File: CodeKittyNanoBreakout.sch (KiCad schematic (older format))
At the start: 13 parts, among them P1 CONN_01X02, P2 CONN_01X02, P3 CONN_01X03, P4 CONN_01X03, P5 CONN_01X02, SW1 SW_PUSH_SMALL_H, SW2 Switch_SPDT_x2, U1 ArduinoNano

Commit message: ...
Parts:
- removed P5: CONN_01X02, Pin_Headers:Pin_Header_Straight_1x02_Pitch2.54mm, symbol CONN_01X02
- added D2: D, Diodes_SMD:D_SOD-323_HandSoldering, symbol D
- added P5: CONN_01X03, Pin_Headers:Pin_Header_Straight_1x03_Pitch2.54mm, symbol CONN_01X03
- added Q1: MMBT3904, TO_SOT_Packages_SMD:SOT-23, symbol MMBT3904
- added R4: 1K, Resistors_SMD:R_0603_HandSoldering, symbol R
- R1, R2: footprint Resistors_SMD:R_0805_HandSoldering -> Resistors_SMD:R_0603_HandSoldering
- SP1: value SPEAKER -> PIEZO
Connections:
- net 5V: now also P5.2 (P2)
- net BUZZ: now also R4.2; no longer SP1.1
- net GND: now also P5.1 (P1), Q1.2 (E); no longer SP1.2
- net VCC: now also SP1.1, D2.1 (K)
- net SENS: now reaches U1.20 (A1)
- net SENS: now also P5.3 (P3)
- new net: D2.2 (A), Q1.3 (C), SP1.2
- new net: Q1.1 (B), R4.1
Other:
- note added: "SENSORS"
- moved on the sheet: SP1
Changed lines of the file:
@@
 F 0 "R2" V 6755 1650 50  0000 C CNN
 F 1 "R" V 6675 1650 50  0000 C CNN
-F 2 "Resistors_SMD:R_0805_HandSoldering" V 6605 1650 50  0001 C CNN
+F 2 "Resistors_SMD:R_0603_HandSoldering" V 6605 1650 50  0001 C CNN
 F 3 "" H 6675 1650 50  0000 C CNN
 	1    6675 1650
@@
 Text GLabel 2550 1675 2    39   Input ~ 0
 VCC
-$Comp
-L CONN_01X02 P5
-U 1 1 597FDB7A
-P 8475 1350
-F 0 "P5" H 8475 1500 50  0000 C CNN
-F 1 "CONN_01X02" V 8575 1350 50  0000 C CNN
-F 2 "Pin_Headers:Pin_Header_Straight_1x02_Pitch2.54mm" H 8475 1350 50  0001 C CNN
-F 3 "" H 8475 1350 50  0000 C CNN
-	1    8475 1350
-	0    -1   -1   0
-$EndComp
-Text GLabel 8425 1550 3    39   Input ~ 0
-GND
-Text GLabel 8900 1675 2    39   Input ~ 0
-BUZZ
-Text Notes 7875 1125 0    197  ~ 0
+Text GLabel 8750 3175 0    39   Input ~ 0
+GND
+Text Notes 8225 875  0    197  ~ 0
 SPEAKER
 $Comp
@@
 F 0 "R1" V 2030 3800 50  0000 C CNN
 F 1 "R" V 1950 3800 50  0000 C CNN
-F 2 "Resistors_SMD:R_0805_HandSoldering" V 1880 3800 50  0001 C CNN
+F 2 "Resistors_SMD:R_0603_HandSoldering" V 1880 3800 50  0001 C CNN
 F 3 "" H 1950 3800 50  0000 C CNN
 	1    1950 3800
@@
 Wire Wire Line
 	1950 3525 1850 3525
-Wire Wire Line
-	8525 1675 8900 1675
-Wire Wire Line
-	8525 1675 8525 1550
 Text GLabel 1575 1575 3    39   Input ~ 0
 GND
@@
 L SPEAKER SP1
 U 1 1 59DC25FB
-P 8925 2350
-F 0 "SP1" H 8825 2600 50  0000 C CNN
-F 1 "SPEAKER" H 8825 2100 50  0000 C CNN
-F 2 "DM_Custom:DM_PiezSMD_PMKCS0909E4000-R1" H 8925 2350 50  0001 C CNN
-F 3 "" H 8925 2350 50  0000 C CNN
-	1    8925 2350
-	1    0    0    -1
-$EndComp
-Text GLabel 8625 2250 0    39   Input ~ 0
+P 9975 1550
+F 0 "SP1" H 9875 1800 50  0000 C CNN
+F 1 "PIEZO" H 9875 1300 50  0000 C CNN
+F 2 "DM_Custom:DM_PiezSMD_PMKCS0909E4000-R1" H 9975 1550 50  0001 C CNN
+F 3 "" H 9975 1550 50  0000 C CNN
+	1    9975 1550
+	1    0    0    -1
+$EndComp
+Text GLabel 8450 2100 0    39   Input ~ 0
 BUZZ
-Text GLabel 8625 2450 0    39   Input ~ 0
+Text GLabel 8450 2450 0    39   Input ~ 0
 GND
 $Comp
@@
 Text GLabel 1825 2475 2    39   Input ~ 0
 GND
+$Comp
+L CONN_01X03 P5
+U 1 1 59FFB57F
+P 8950 3275
+F 0 "P5" H 8950 3475 50  0000 C CNN
+F 1 "CONN_01X03" V 9050 3275 50  0000 C CNN
+F 2 "Pin_Headers:Pin_Header_Straight_1x03_Pitch2.54mm" H 8950 3275 50  0001 C CNN
+F 3 "" H 8950 3275 50  0000 C CNN
+	1    8950 3275
+	1    0    0    -1
+$EndComp
+Text GLabel 8750 3275 0    39   Input ~ 0
+5V
+Text GLabel 8750 3375 0    39   Input ~ 0
+SENS
+Text GLabel 4750 3100 2    39   Input ~ 0
+SENS
+Text Notes 7925 2950 0    197  ~ 0
+SENSORS
+Text GLabel 8425 1300 0    39   Input ~ 0
+VCC
+$Comp
+L D D2
+U 1 1 5A0CCEA3
+P 9150 1650
+F 0 "D2" H 9150 1750 50  0000 C CNN
+F 1 "D" H 9150 1550 50  0000 C CNN
+F 2 "Diodes_SMD:D_SOD-323_HandSoldering" H 9150 1650 50  0001 C CNN
+F 3 "" H 9150 1650 50  0000 C CNN
+	1    9150 1650
+	1    0    0    -1
+$EndComp
+$Comp
+L R R4
+U 1 1 5A0CD00D
+P 8875 2100
+F 0 "R4" V 8955 2100 50  0000 C CNN
+F 1 "1K" V 8875 2100 50  0000 C CNN
+F 2 "Resistors_SMD:R_0603_HandSoldering" V 8805 2100 50  0001 C CNN
+F 3 "" H 8875 2100 50  0000 C CNN
+	1    8875 2100
+	0    1    1    0
+$EndComp
+$Comp
+L MMBT3904 Q1
+U 1 1 5A0CD092
+P 9325 2100
+F 0 "Q1" H 9525 2175 50  0000 L CNN
+F 1 "MMBT3904" H 9525 2100 50  0000 L CNN
+F 2 "TO_SOT_Packages_SMD:SOT-23" H 9525 2025 50  0000 L CIN
+F 3 "" H 9325 2100 50  0000 L CNN
+	1    9325 2100
+	1    0    0    -1
+$EndComp
+Wire Wire Line
+	8450 2450 9425 2450
+Wire Wire Line
+	9425 2450 9425 2300
+Wire Wire Line
+	9025 2100 9125 2100
+Wire Wire Line
+	8450 2100 8725 2100
+Wire Wire Line
+	9675 1650 9300 1650
+Wire Wire Line
+	9425 1900 9425 1650
+Connection ~ 9425 1650
+Wire Wire Line
+	8675 1650 9000 1650
+Wire Wire Line
+	8675 1325 8675 1650
+Wire Wire Line
+	8675 1325 9675 1325
+Wire Wire Line
+	9675 1325 9675 1450
+Wire Wire Line
+	8425 1300 9275 1300
+Wire Wire Line
+	9275 1300 9275 1325
+Connection ~ 9275 1325
 $EndSCHEMATC

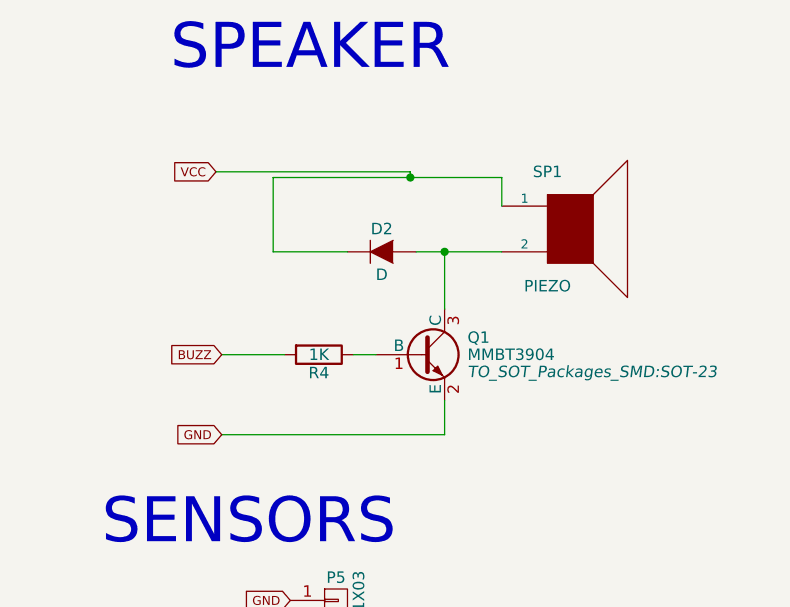
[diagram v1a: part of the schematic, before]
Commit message: removed driver from piezo -- direct drive baby!
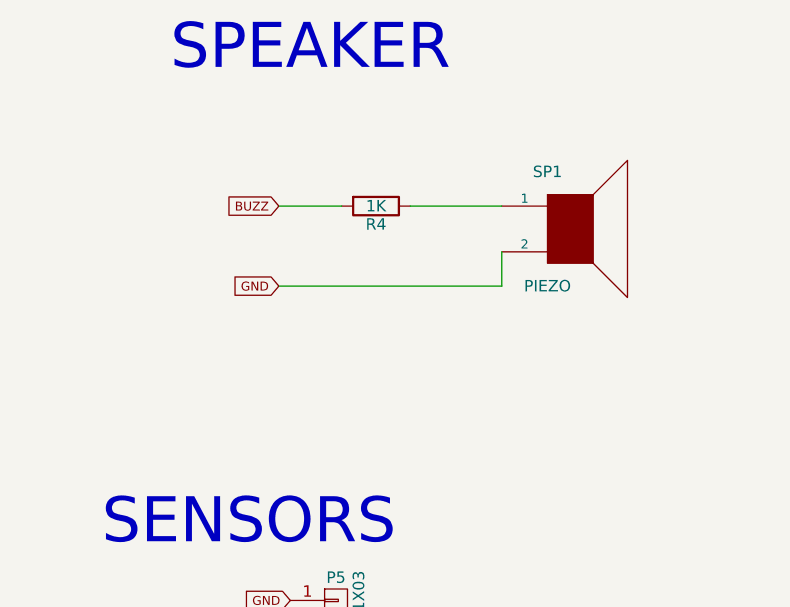
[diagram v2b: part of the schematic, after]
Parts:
- removed D2: D, Diodes_SMD:D_SOD-323_HandSoldering, symbol D
- removed Q1: MMBT3904, TO_SOT_Packages_SMD:SOT-23, symbol MMBT3904
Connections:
- net GND: now also SP1.2
- net VCC: no longer SP1.1
- net at R4.1: now also SP1.1
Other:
- moved on the sheet: R4
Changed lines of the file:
@@
 EESchema Schematic File Version 2
+LIBS:CodeKittyNanoBreakout-rescue
 LIBS:power
 LIBS:device
@@
 	1    0    0    -1
 $EndComp
-Text GLabel 8450 2100 0    39   Input ~ 0
+Text GLabel 8700 1450 0    39   Input ~ 0
 BUZZ
-Text GLabel 8450 2450 0    39   Input ~ 0
+Text GLabel 8700 1800 0    39   Input ~ 0
 GND
 $Comp
@@
 Text Notes 7925 2950 0    197  ~ 0
 SENSORS
-Text GLabel 8425 1300 0    39   Input ~ 0
-VCC
-$Comp
-L D D2
-U 1 1 5A0CCEA3
-P 9150 1650
-F 0 "D2" H 9150 1750 50  0000 C CNN
-F 1 "D" H 9150 1550 50  0000 C CNN
-F 2 "Diodes_SMD:D_SOD-323_HandSoldering" H 9150 1650 50  0001 C CNN
-F 3 "" H 9150 1650 50  0000 C CNN
-	1    9150 1650
-	1    0    0    -1
-$EndComp
 $Comp
 L R R4
 U 1 1 5A0CD00D
-P 8875 2100
-F 0 "R4" V 8955 2100 50  0000 C CNN
-F 1 "1K" V 8875 2100 50  0000 C CNN
-F 2 "Resistors_SMD:R_0603_HandSoldering" V 8805 2100 50  0001 C CNN
-F 3 "" H 8875 2100 50  0000 C CNN
-	1    8875 2100
+P 9125 1450
+F 0 "R4" V 9205 1450 50  0000 C CNN
+F 1 "1K" V 9125 1450 50  0000 C CNN
+F 2 "Resistors_SMD:R_0603_HandSoldering" V 9055 1450 50  0001 C CNN
+F 3 "" H 9125 1450 50  0000 C CNN
+	1    9125 1450
 	0    1    1    0
 $EndComp
-$Comp
-L MMBT3904 Q1
-U 1 1 5A0CD092
-P 9325 2100
-F 0 "Q1" H 9525 2175 50  0000 L CNN
-F 1 "MMBT3904" H 9525 2100 50  0000 L CNN
-F 2 "TO_SOT_Packages_SMD:SOT-23" H 9525 2025 50  0000 L CIN
-F 3 "" H 9325 2100 50  0000 L CNN
-	1    9325 2100
-	1    0    0    -1
-$EndComp
-Wire Wire Line
-	8450 2450 9425 2450
-Wire Wire Line
-	9425 2450 9425 2300
-Wire Wire Line
-	9025 2100 9125 2100
-Wire Wire Line
-	8450 2100 8725 2100
-Wire Wire Line
-	9675 1650 9300 1650
-Wire Wire Line
-	9425 1900 9425 1650
-Connection ~ 9425 1650
-Wire Wire Line
-	8675 1650 9000 1650
-Wire Wire Line
-	8675 1325 8675 1650
-Wire Wire Line
-	8675 1325 9675 1325
-Wire Wire Line
-	9675 1325 9675 1450
-Wire Wire Line
-	8425 1300 9275 1300
-Wire Wire Line
-	9275 1300 9275 1325
-Connection ~ 9275 1325
+Wire Wire Line
+	8700 1800 9675 1800
+Wire Wire Line
+	9675 1800 9675 1650
+Wire Wire Line
+	9275 1450 9675 1450
+Wire Wire Line
+	8700 1450 8975 1450
 $EndSCHEMATC
